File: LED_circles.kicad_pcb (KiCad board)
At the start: 2 copper layers, 125 x 125 mm, 72 parts

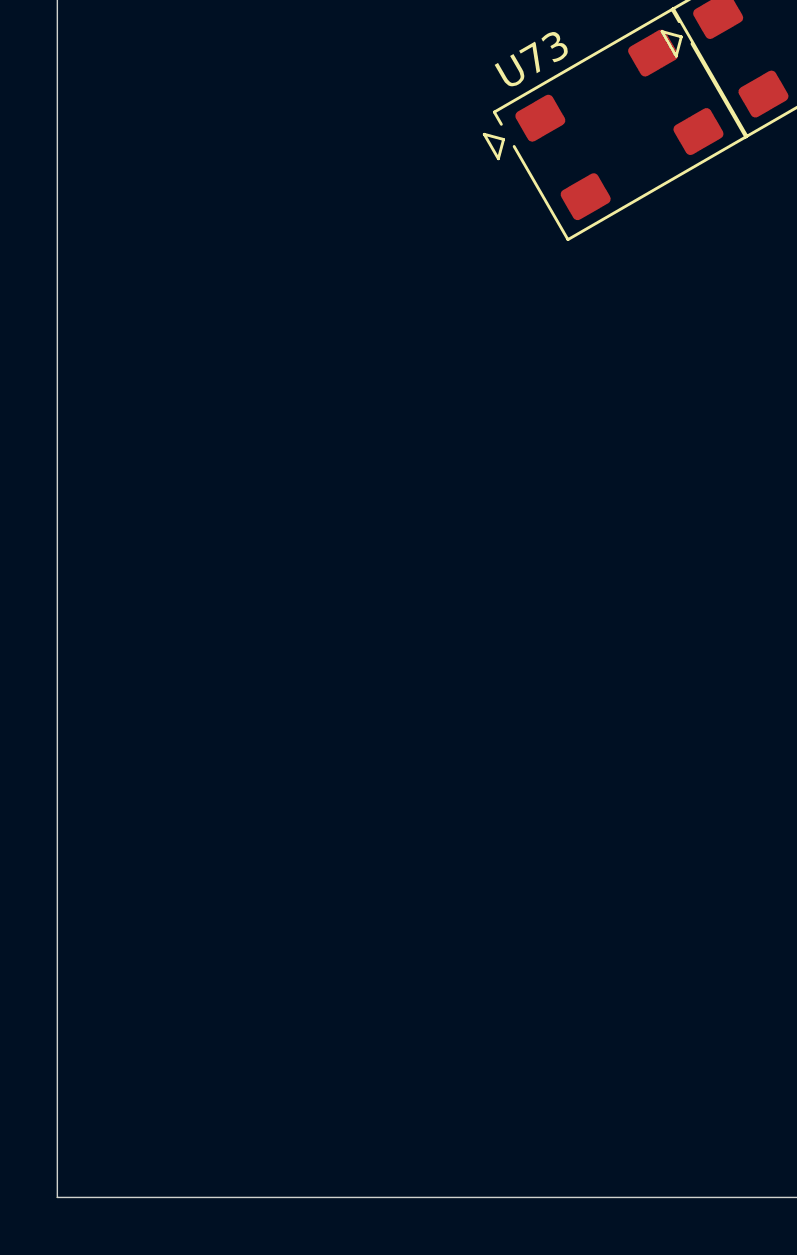
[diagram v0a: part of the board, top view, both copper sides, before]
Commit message: Initial Schematic and LED Placement
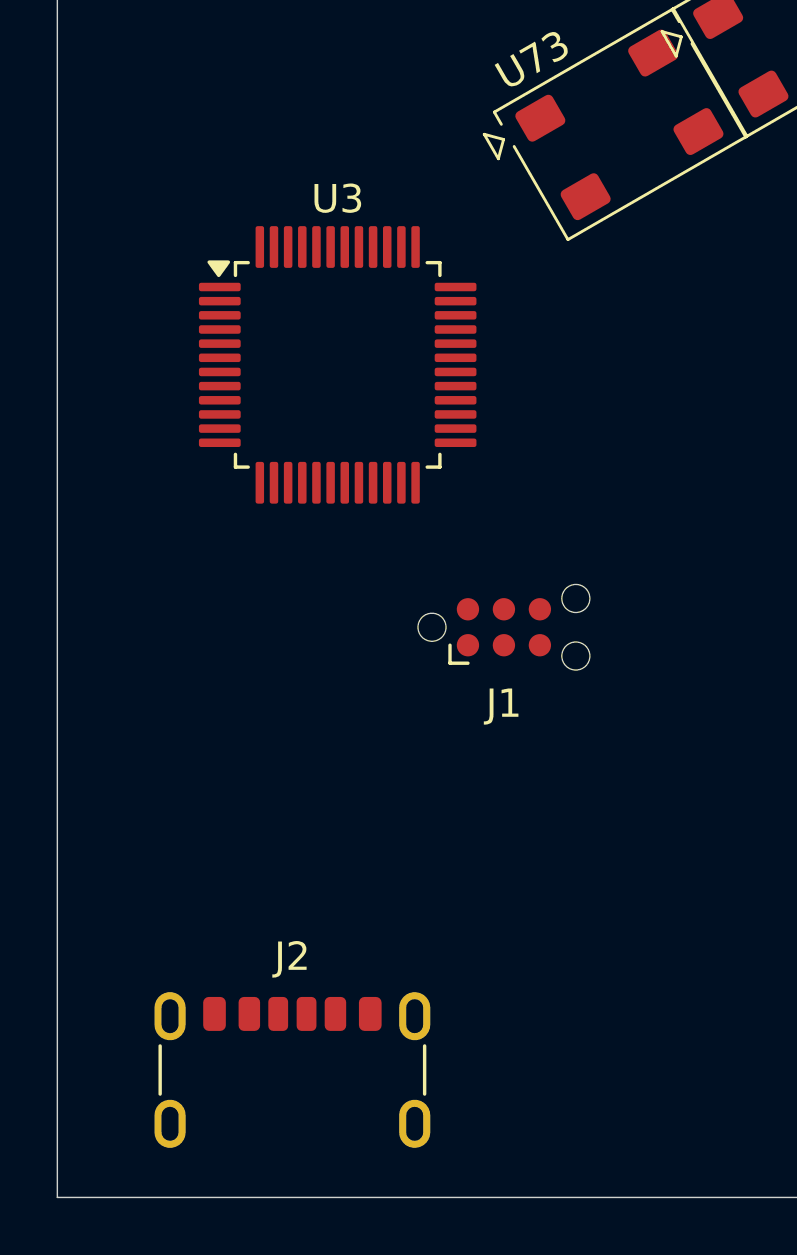
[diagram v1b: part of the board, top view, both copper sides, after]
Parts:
- added J1: Conn_ARM_SWD_TagConnect_TC2030-NL, Connector:Tag-Connect_TC2030-IDC-NL_2x03_P1.27mm_Vertical, F.Cu at (96.8, 142.4)
- added J2: USB_C_Receptacle_PowerOnly_6P, Connector_USB:USB_C_Receptacle_GCT_USB4125-xx-x-0190_6P_TopMnt_Horizontal, F.Cu at (89.3, 159.1)
- added U3: STM32F070CBTx, Package_QFP:LQFP-48_7x7mm_P0.5mm, F.Cu at (90.9, 133.1)
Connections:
- net /Row1/DIN_{TOP} renamed Net-(U1-DIN)
- net /Row6/DOUT_{BOTTOM} renamed Net-(U73-DOUT)
- U1 pad 1: unconnected-(U1-GND-Pad1) -> GND
- U1 pad 4: unconnected-(U1-VDD-Pad4) -> +5V
- U10 pad 1: unconnected-(U10-GND-Pad1) -> GND
- U10 pad 4: unconnected-(U10-VDD-Pad4) -> +5V
- U11 pad 1: unconnected-(U11-GND-Pad1) -> GND
- U11 pad 4: unconnected-(U11-VDD-Pad4) -> +5V
- U12 pad 1: unconnected-(U12-GND-Pad1) -> GND
- U12 pad 4: unconnected-(U12-VDD-Pad4) -> +5V
- U13 pad 1: unconnected-(U13-GND-Pad1) -> GND
- U13 pad 2: /Row1/DOUT_{BOTTOM} -> Net-(U13-DOUT)
- U13 pad 4: unconnected-(U13-VDD-Pad4) -> +5V
- U14 pad 1: unconnected-(U14-GND-Pad1) -> GND
- U14 pad 3: /Row1/DOUT_{TOP} -> Net-(U14-DIN)
- U14 pad 4: unconnected-(U14-VDD-Pad4) -> +5V
- U15 pad 1: unconnected-(U15-GND-Pad1) -> GND
- U15 pad 4: unconnected-(U15-VDD-Pad4) -> +5V
- U16 pad 1: unconnected-(U16-GND-Pad1) -> GND
- U16 pad 4: unconnected-(U16-VDD-Pad4) -> +5V
- U17 pad 1: unconnected-(U17-GND-Pad1) -> GND
- U17 pad 4: unconnected-(U17-VDD-Pad4) -> +5V
- U18 pad 1: unconnected-(U18-GND-Pad1) -> GND
- U18 pad 4: unconnected-(U18-VDD-Pad4) -> +5V
- U19 pad 1: unconnected-(U19-GND-Pad1) -> GND
- U19 pad 2: /Row2/DOUT_{TOP} -> Net-(U19-DOUT)
- U19 pad 4: unconnected-(U19-VDD-Pad4) -> +5V
- U2 pad 1: unconnected-(U2-GND-Pad1) -> GND
- U2 pad 4: unconnected-(U2-VDD-Pad4) -> +5V
- U20 pad 1: unconnected-(U20-GND-Pad1) -> GND
- U20 pad 3: /Row1/DOUT_{BOTTOM} -> Net-(U20-DIN)
- U20 pad 4: unconnected-(U20-VDD-Pad4) -> +5V
- U21 pad 1: unconnected-(U21-GND-Pad1) -> GND
- U21 pad 4: unconnected-(U21-VDD-Pad4) -> +5V
- U22 pad 1: unconnected-(U22-GND-Pad1) -> GND
- U22 pad 4: unconnected-(U22-VDD-Pad4) -> +5V
- U23 pad 1: unconnected-(U23-GND-Pad1) -> GND
- U23 pad 4: unconnected-(U23-VDD-Pad4) -> +5V
- U24 pad 1: unconnected-(U24-GND-Pad1) -> GND
- U24 pad 4: unconnected-(U24-VDD-Pad4) -> +5V
- U25 pad 1: unconnected-(U25-GND-Pad1) -> GND
- U25 pad 2: /Row2/DOUT_{BOTTOM} -> Net-(U25-DOUT)
- U25 pad 4: unconnected-(U25-VDD-Pad4) -> +5V
- U26 pad 1: unconnected-(U26-GND-Pad1) -> GND
- U26 pad 3: /Row2/DOUT_{TOP} -> Net-(U26-DIN)
- U26 pad 4: unconnected-(U26-VDD-Pad4) -> +5V
- U27 pad 1: unconnected-(U27-GND-Pad1) -> GND
- U27 pad 4: unconnected-(U27-VDD-Pad4) -> +5V
- U28 pad 1: unconnected-(U28-GND-Pad1) -> GND
- U28 pad 4: unconnected-(U28-VDD-Pad4) -> +5V
- U29 pad 1: unconnected-(U29-GND-Pad1) -> GND
- U29 pad 4: unconnected-(U29-VDD-Pad4) -> +5V
- U30 pad 1: unconnected-(U30-GND-Pad1) -> GND
- U30 pad 4: unconnected-(U30-VDD-Pad4) -> +5V
- U31 pad 1: unconnected-(U31-GND-Pad1) -> GND
- U31 pad 2: /Row3/DOUT_{TOP} -> Net-(U31-DOUT)
- U31 pad 4: unconnected-(U31-VDD-Pad4) -> +5V
- U32 pad 1: unconnected-(U32-GND-Pad1) -> GND
- U32 pad 3: /Row2/DOUT_{BOTTOM} -> Net-(U32-DIN)
- U32 pad 4: unconnected-(U32-VDD-Pad4) -> +5V
- U33 pad 1: unconnected-(U33-GND-Pad1) -> GND
- U33 pad 4: unconnected-(U33-VDD-Pad4) -> +5V
- U34 pad 1: unconnected-(U34-GND-Pad1) -> GND
- U34 pad 4: unconnected-(U34-VDD-Pad4) -> +5V
- U35 pad 1: unconnected-(U35-GND-Pad1) -> GND
- U35 pad 4: unconnected-(U35-VDD-Pad4) -> +5V
- U36 pad 1: unconnected-(U36-GND-Pad1) -> GND
- U36 pad 4: unconnected-(U36-VDD-Pad4) -> +5V
- U37 pad 1: unconnected-(U37-GND-Pad1) -> GND
- U37 pad 2: /Row3/DOUT_{BOTTOM} -> Net-(U37-DOUT)
- U37 pad 4: unconnected-(U37-VDD-Pad4) -> +5V
- U38 pad 1: unconnected-(U38-GND-Pad1) -> GND
- U38 pad 3: /Row3/DOUT_{TOP} -> Net-(U38-DIN)
- U38 pad 4: unconnected-(U38-VDD-Pad4) -> +5V
- U39 pad 1: unconnected-(U39-GND-Pad1) -> GND
- U39 pad 4: unconnected-(U39-VDD-Pad4) -> +5V
- U4 pad 1: unconnected-(U4-GND-Pad1) -> GND
- U4 pad 4: unconnected-(U4-VDD-Pad4) -> +5V
- U40 pad 1: unconnected-(U40-GND-Pad1) -> GND
- U40 pad 4: unconnected-(U40-VDD-Pad4) -> +5V
- U41 pad 1: unconnected-(U41-GND-Pad1) -> GND
- U41 pad 4: unconnected-(U41-VDD-Pad4) -> +5V
- U42 pad 1: unconnected-(U42-GND-Pad1) -> GND
- U42 pad 4: unconnected-(U42-VDD-Pad4) -> +5V
- U43 pad 1: unconnected-(U43-GND-Pad1) -> GND
- U43 pad 2: /Row4/DOUT_{TOP} -> Net-(U43-DOUT)
- U43 pad 4: unconnected-(U43-VDD-Pad4) -> +5V
- U44 pad 1: unconnected-(U44-GND-Pad1) -> GND
- U44 pad 3: /Row3/DOUT_{BOTTOM} -> Net-(U44-DIN)
- U44 pad 4: unconnected-(U44-VDD-Pad4) -> +5V
- U45 pad 1: unconnected-(U45-GND-Pad1) -> GND
- U45 pad 4: unconnected-(U45-VDD-Pad4) -> +5V
- U46 pad 1: unconnected-(U46-GND-Pad1) -> GND
- U46 pad 4: unconnected-(U46-VDD-Pad4) -> +5V
- U47 pad 1: unconnected-(U47-GND-Pad1) -> GND
- U47 pad 4: unconnected-(U47-VDD-Pad4) -> +5V
- U48 pad 1: unconnected-(U48-GND-Pad1) -> GND
- U48 pad 4: unconnected-(U48-VDD-Pad4) -> +5V
- U49 pad 1: unconnected-(U49-GND-Pad1) -> GND
- U49 pad 2: /Row4/DOUT_{BOTTOM} -> Net-(U49-DOUT)
- U49 pad 4: unconnected-(U49-VDD-Pad4) -> +5V
- U5 pad 1: unconnected-(U5-GND-Pad1) -> GND
- U5 pad 4: unconnected-(U5-VDD-Pad4) -> +5V
- U50 pad 1: unconnected-(U50-GND-Pad1) -> GND
- U50 pad 3: /Row4/DOUT_{TOP} -> Net-(U50-DIN)
- U50 pad 4: unconnected-(U50-VDD-Pad4) -> +5V
- U51 pad 1: unconnected-(U51-GND-Pad1) -> GND
- U51 pad 4: unconnected-(U51-VDD-Pad4) -> +5V
- U52 pad 1: unconnected-(U52-GND-Pad1) -> GND
- U52 pad 4: unconnected-(U52-VDD-Pad4) -> +5V
- U53 pad 1: unconnected-(U53-GND-Pad1) -> GND
- U53 pad 4: unconnected-(U53-VDD-Pad4) -> +5V
- U54 pad 1: unconnected-(U54-GND-Pad1) -> GND
- U54 pad 4: unconnected-(U54-VDD-Pad4) -> +5V
- U55 pad 1: unconnected-(U55-GND-Pad1) -> GND
- U55 pad 2: /Row5/DOUT_{TOP} -> Net-(U55-DOUT)
- U55 pad 4: unconnected-(U55-VDD-Pad4) -> +5V
- U56 pad 1: unconnected-(U56-GND-Pad1) -> GND
- U56 pad 3: /Row4/DOUT_{BOTTOM} -> Net-(U56-DIN)
- U56 pad 4: unconnected-(U56-VDD-Pad4) -> +5V
- U57 pad 1: unconnected-(U57-GND-Pad1) -> GND
- U57 pad 4: unconnected-(U57-VDD-Pad4) -> +5V
- U58 pad 1: unconnected-(U58-GND-Pad1) -> GND
- U58 pad 4: unconnected-(U58-VDD-Pad4) -> +5V
- U59 pad 1: unconnected-(U59-GND-Pad1) -> GND
- U59 pad 4: unconnected-(U59-VDD-Pad4) -> +5V
- U6 pad 1: unconnected-(U6-GND-Pad1) -> GND
- U6 pad 4: unconnected-(U6-VDD-Pad4) -> +5V
- U60 pad 1: unconnected-(U60-GND-Pad1) -> GND
- U60 pad 4: unconnected-(U60-VDD-Pad4) -> +5V
- U61 pad 1: unconnected-(U61-GND-Pad1) -> GND
- U61 pad 2: /Row5/DOUT_{BOTTOM} -> Net-(U61-DOUT)
- U61 pad 4: unconnected-(U61-VDD-Pad4) -> +5V
- U62 pad 1: unconnected-(U62-GND-Pad1) -> GND
- U62 pad 3: /Row5/DOUT_{TOP} -> Net-(U62-DIN)
- U62 pad 4: unconnected-(U62-VDD-Pad4) -> +5V
- U63 pad 1: unconnected-(U63-GND-Pad1) -> GND
- U63 pad 4: unconnected-(U63-VDD-Pad4) -> +5V
- U64 pad 1: unconnected-(U64-GND-Pad1) -> GND
- U64 pad 4: unconnected-(U64-VDD-Pad4) -> +5V
- U65 pad 1: unconnected-(U65-GND-Pad1) -> GND
- U65 pad 4: unconnected-(U65-VDD-Pad4) -> +5V
- U66 pad 1: unconnected-(U66-GND-Pad1) -> GND
- U66 pad 4: unconnected-(U66-VDD-Pad4) -> +5V
- U67 pad 1: unconnected-(U67-GND-Pad1) -> GND
- U67 pad 2: /Row1/DIN_{BOTTOM} -> Net-(U67-DOUT)
- U67 pad 4: unconnected-(U67-VDD-Pad4) -> +5V
- U68 pad 1: unconnected-(U68-GND-Pad1) -> GND
- U68 pad 3: /Row5/DOUT_{BOTTOM} -> Net-(U68-DIN)
- U68 pad 4: unconnected-(U68-VDD-Pad4) -> +5V
- U69 pad 1: unconnected-(U69-GND-Pad1) -> GND
- U69 pad 4: unconnected-(U69-VDD-Pad4) -> +5V
- U7 pad 1: unconnected-(U7-GND-Pad1) -> GND
- U7 pad 2: /Row1/DOUT_{TOP} -> Net-(U7-DOUT)
- U7 pad 4: unconnected-(U7-VDD-Pad4) -> +5V
- U70 pad 1: unconnected-(U70-GND-Pad1) -> GND
- U70 pad 4: unconnected-(U70-VDD-Pad4) -> +5V
- U71 pad 1: unconnected-(U71-GND-Pad1) -> GND
- U71 pad 4: unconnected-(U71-VDD-Pad4) -> +5V
- U72 pad 1: unconnected-(U72-GND-Pad1) -> GND
- U72 pad 4: unconnected-(U72-VDD-Pad4) -> +5V
- U73 pad 1: unconnected-(U73-GND-Pad1) -> GND
- U73 pad 4: unconnected-(U73-VDD-Pad4) -> +5V
- U8 pad 1: unconnected-(U8-GND-Pad1) -> GND
- U8 pad 3: /Row1/DIN_{BOTTOM} -> Net-(U8-DIN)
- U8 pad 4: unconnected-(U8-VDD-Pad4) -> +5V
- U9 pad 1: unconnected-(U9-GND-Pad1) -> GND
- U9 pad 4: unconnected-(U9-VDD-Pad4) -> +5V
